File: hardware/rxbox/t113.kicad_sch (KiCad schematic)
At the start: 1 part, among them U1 T113-I

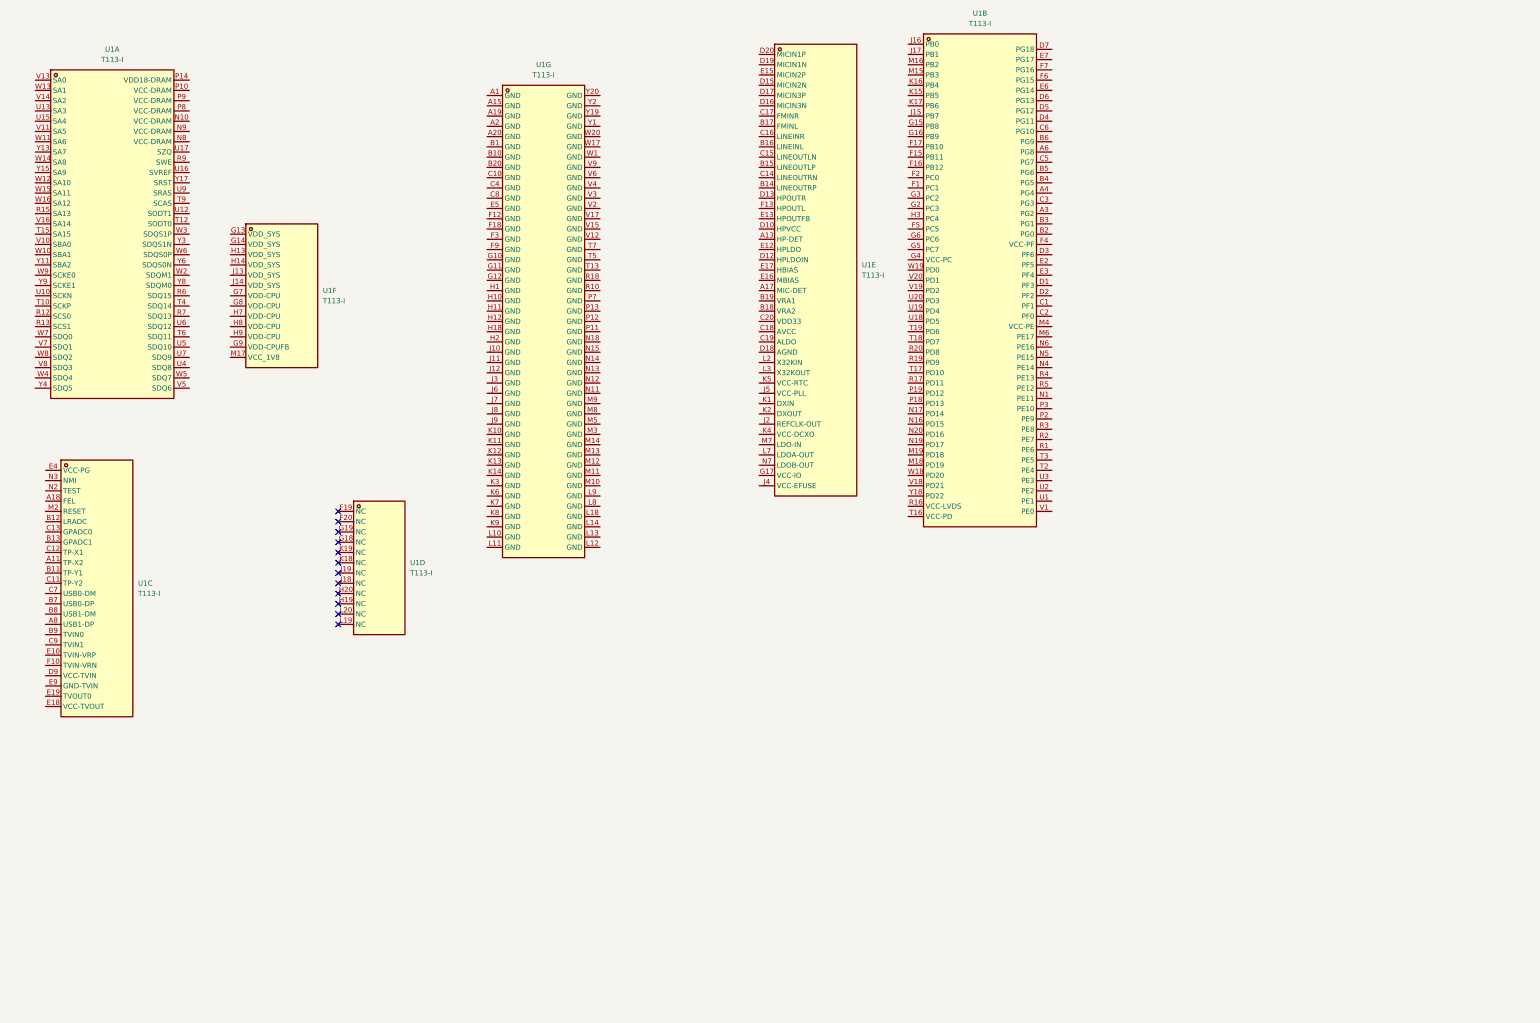
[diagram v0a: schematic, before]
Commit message: connect power + t113 sheets
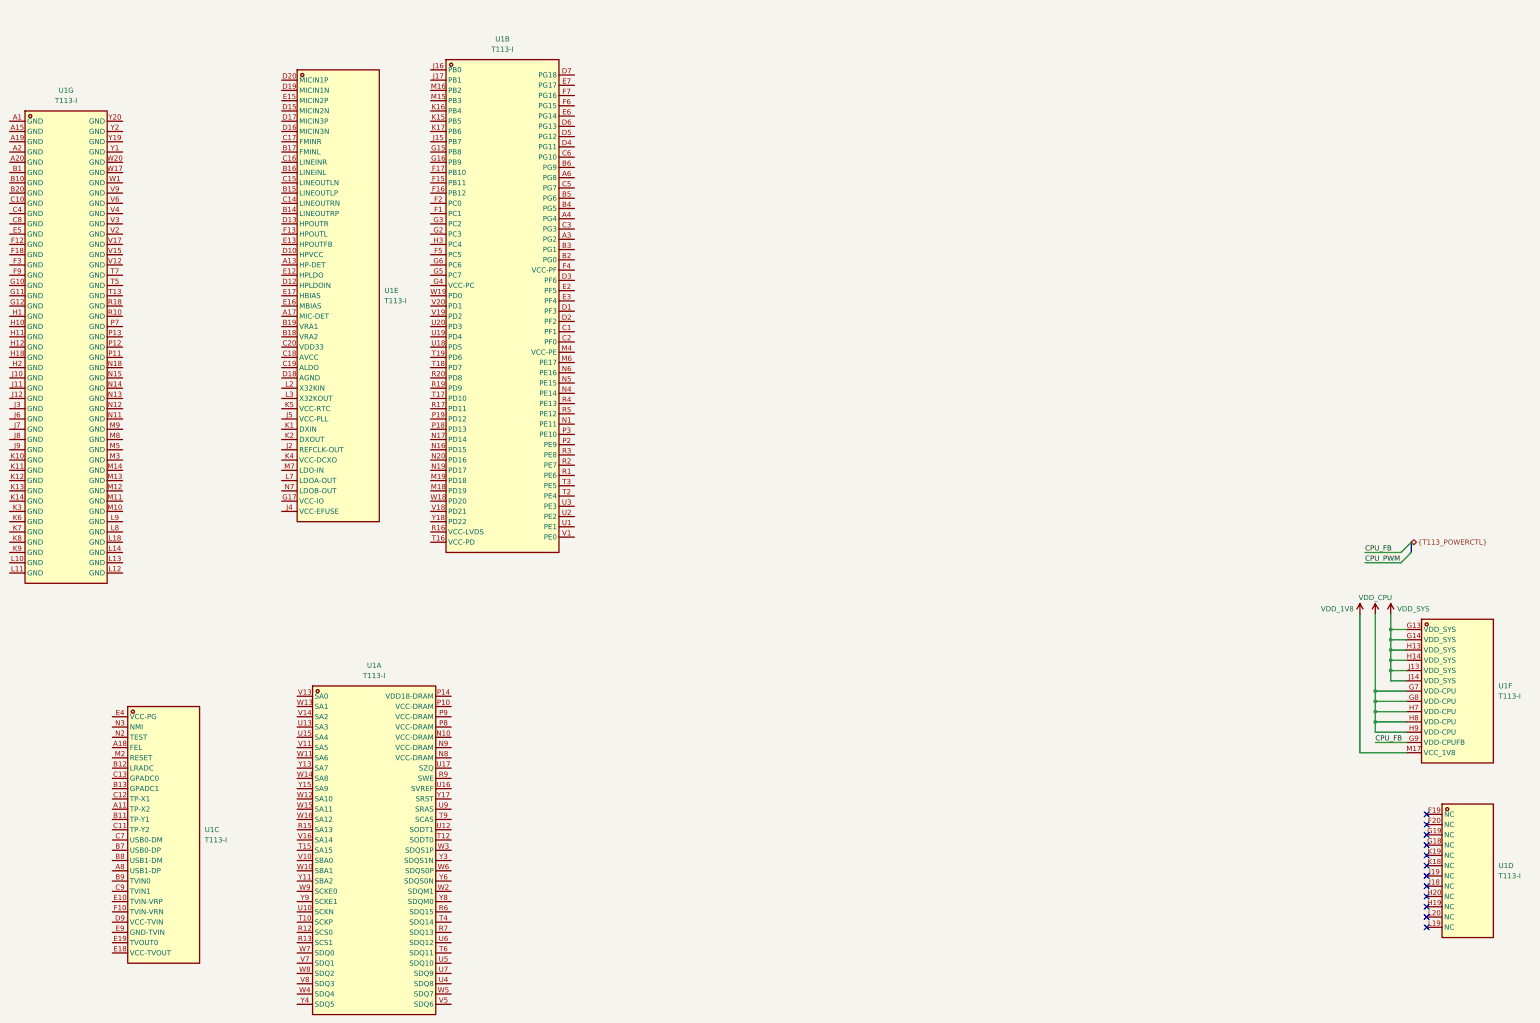
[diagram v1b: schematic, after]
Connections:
- net VDD_SYS: now reaches U1.G13 (VDD_SYS)
- net VDD_SYS: now also U1.G14 (VDD_SYS), U1.H13 (VDD_SYS), U1.H14 (VDD_SYS), U1.J13 (VDD_SYS), U1.J14 (VDD_SYS)
- net VDD_CPU: now reaches U1.G7 (VDD-CPU)
- net VDD_CPU: now also U1.G8 (VDD-CPU), U1.H7 (VDD-CPU), U1.H8 (VDD-CPU), U1.H9 (VDD-CPU)
- net CPU_FB: now reaches U1.G9 (VDD-CPUFB)
- net VDD_1V8: now reaches U1.M17 (VCC_1V8)
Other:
- moved on the sheet: U1A, U1B, U1C, U1D, U1E, U1F, U1G

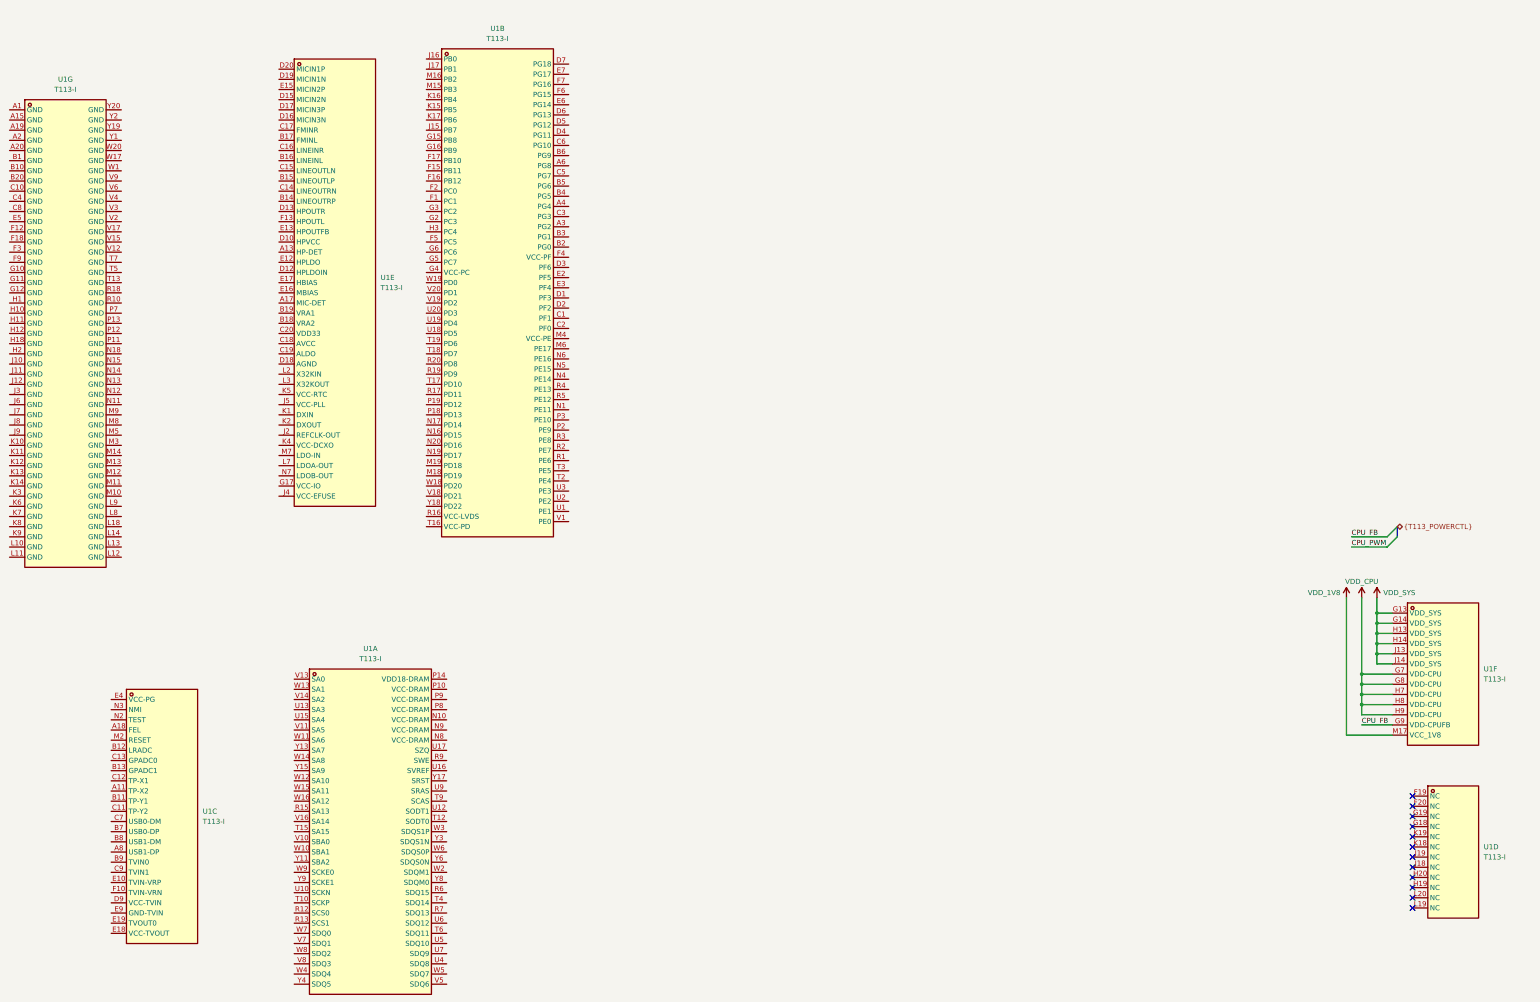
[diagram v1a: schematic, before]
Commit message: finish up power, start wifi
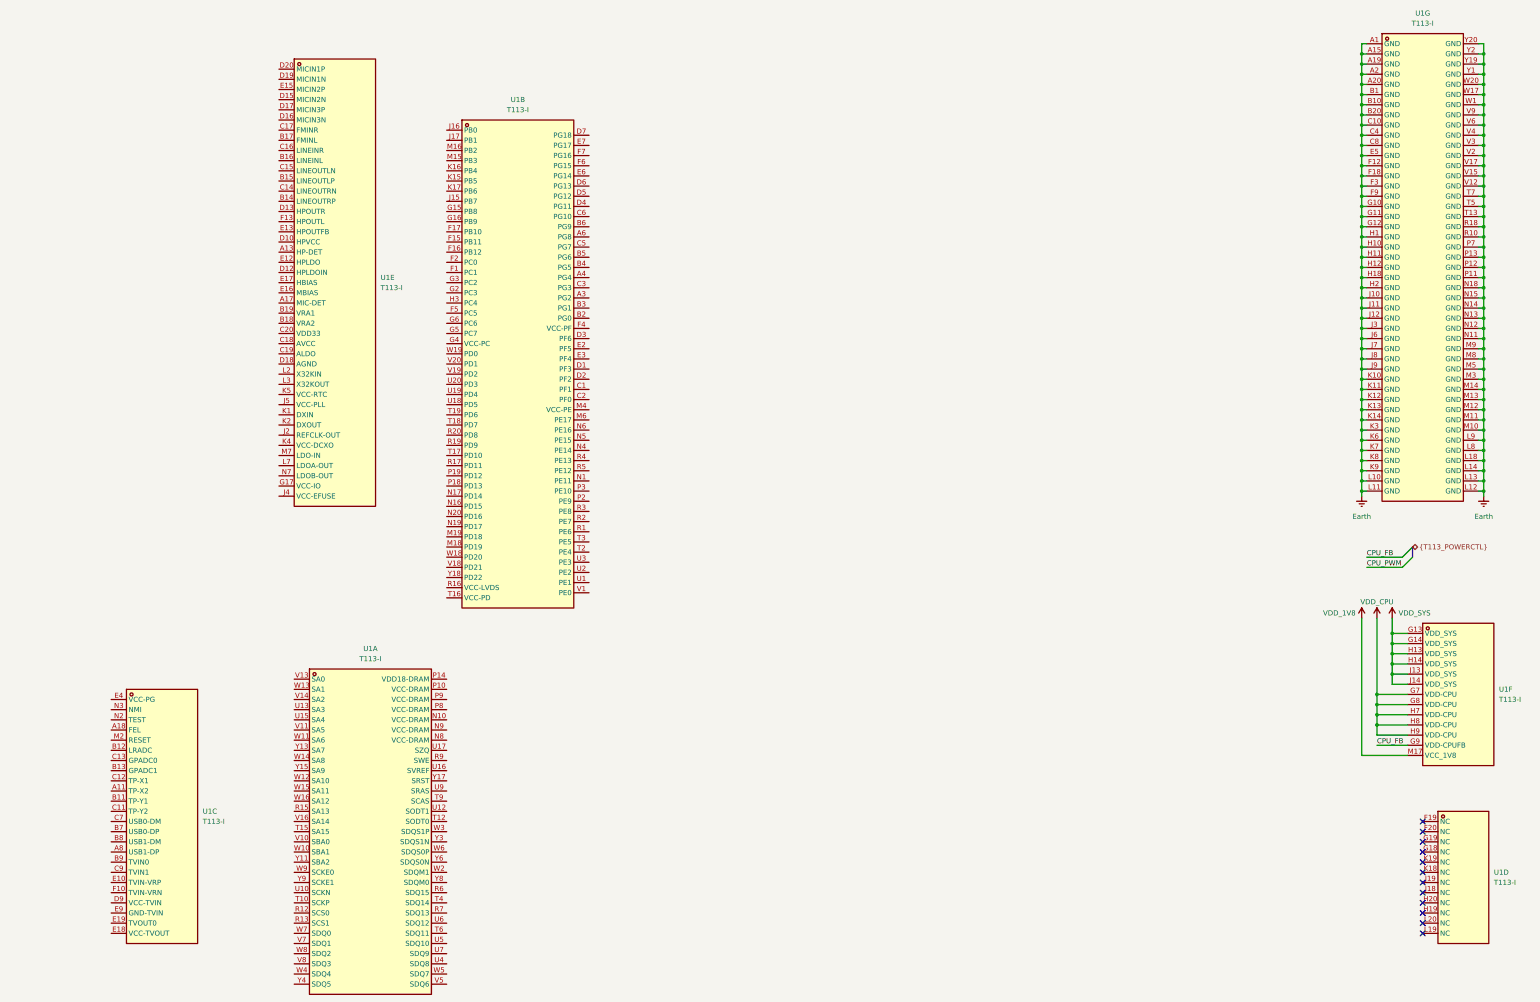
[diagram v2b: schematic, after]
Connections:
- net Earth: now reaches U1.A1 (GND)
- net Earth: now also U1.A15 (GND), U1.A19 (GND), U1.A2 (GND), U1.A20 (GND), U1.B1 (GND), U1.B10 (GND), U1.B20 (GND), U1.C10 (GND), U1.C4 (GND), U1.C8 (GND), U1.E5 (GND), U1.F12 (GND), U1.F18 (GND), U1.F3 (GND), U1.F9 (GND), U1.G10 (GND), U1.G11 (GND), U1.G12 (GND), U1.H1 (GND), U1.H10 (GND), U1.H11 (GND), U1.H12 (GND), U1.H18 (GND), U1.H2 (GND), U1.J10 (GND), U1.J11 (GND), U1.J12 (GND), U1.J3 (GND), U1.J6 (GND), U1.J7 (GND), U1.J8 (GND), U1.J9 (GND), U1.K10 (GND), U1.K11 (GND), U1.K12 (GND), U1.K13 (GND), U1.K14 (GND), U1.K3 (GND), U1.K6 (GND), U1.K7 (GND), U1.K8 (GND), U1.K9 (GND), U1.L10 (GND), U1.L11 (GND), U1.L12 (GND), U1.L13 (GND), U1.L14 (GND), U1.L18 (GND), U1.L8 (GND), U1.L9 (GND), U1.M10 (GND), U1.M11 (GND), U1.M12 (GND), U1.M13 (GND), U1.M14 (GND), U1.M3 (GND), U1.M5 (GND), U1.M8 (GND), U1.M9 (GND), U1.N11 (GND), U1.N12 (GND), U1.N13 (GND), U1.N14 (GND), U1.N15 (GND), U1.N18 (GND), U1.P11 (GND), U1.P12 (GND), U1.P13 (GND), U1.P7 (GND), U1.R10 (GND), U1.R18 (GND), U1.T13 (GND), U1.T5 (GND), U1.T7 (GND), U1.V12 (GND), U1.V15 (GND), U1.V17 (GND), U1.V2 (GND), U1.V3 (GND), U1.V4 (GND), U1.V6 (GND), U1.V9 (GND), U1.W1 (GND), U1.W17 (GND), U1.W20 (GND), U1.Y1 (GND), U1.Y19 (GND), U1.Y2 (GND), U1.Y20 (GND)
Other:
- moved on the sheet: U1B, U1D, U1F, U1G

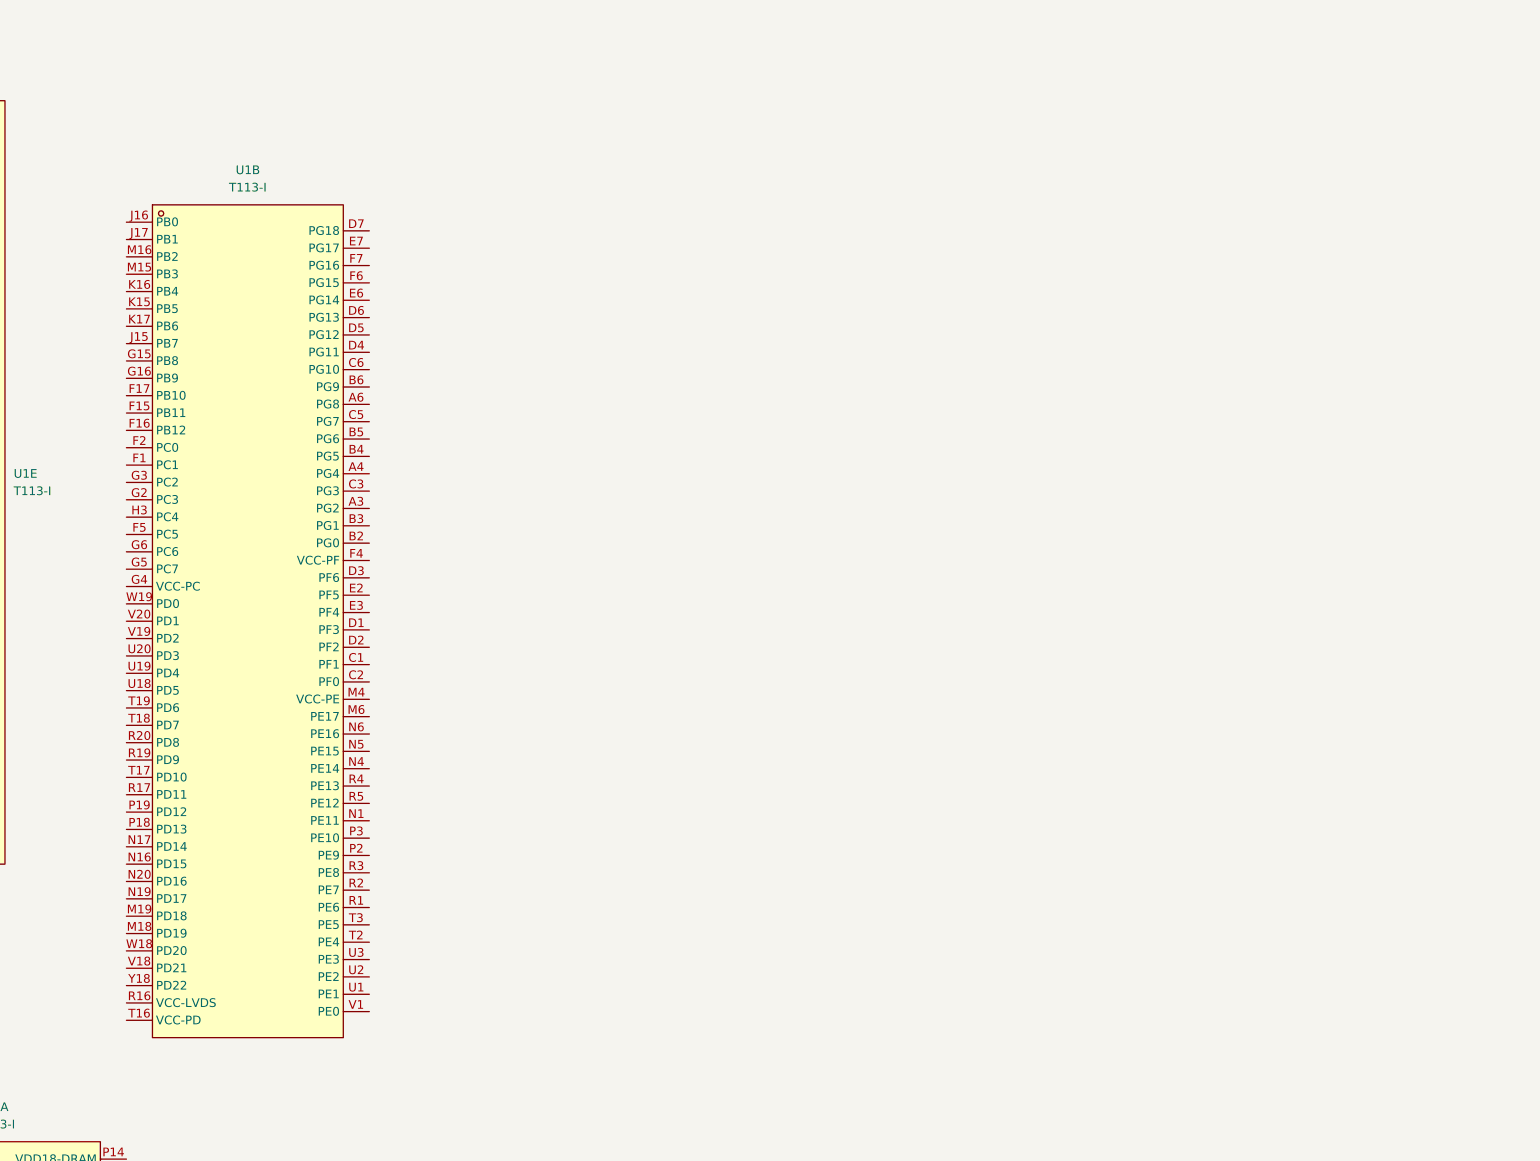
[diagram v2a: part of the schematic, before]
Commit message: wiring wifi + bt to t113
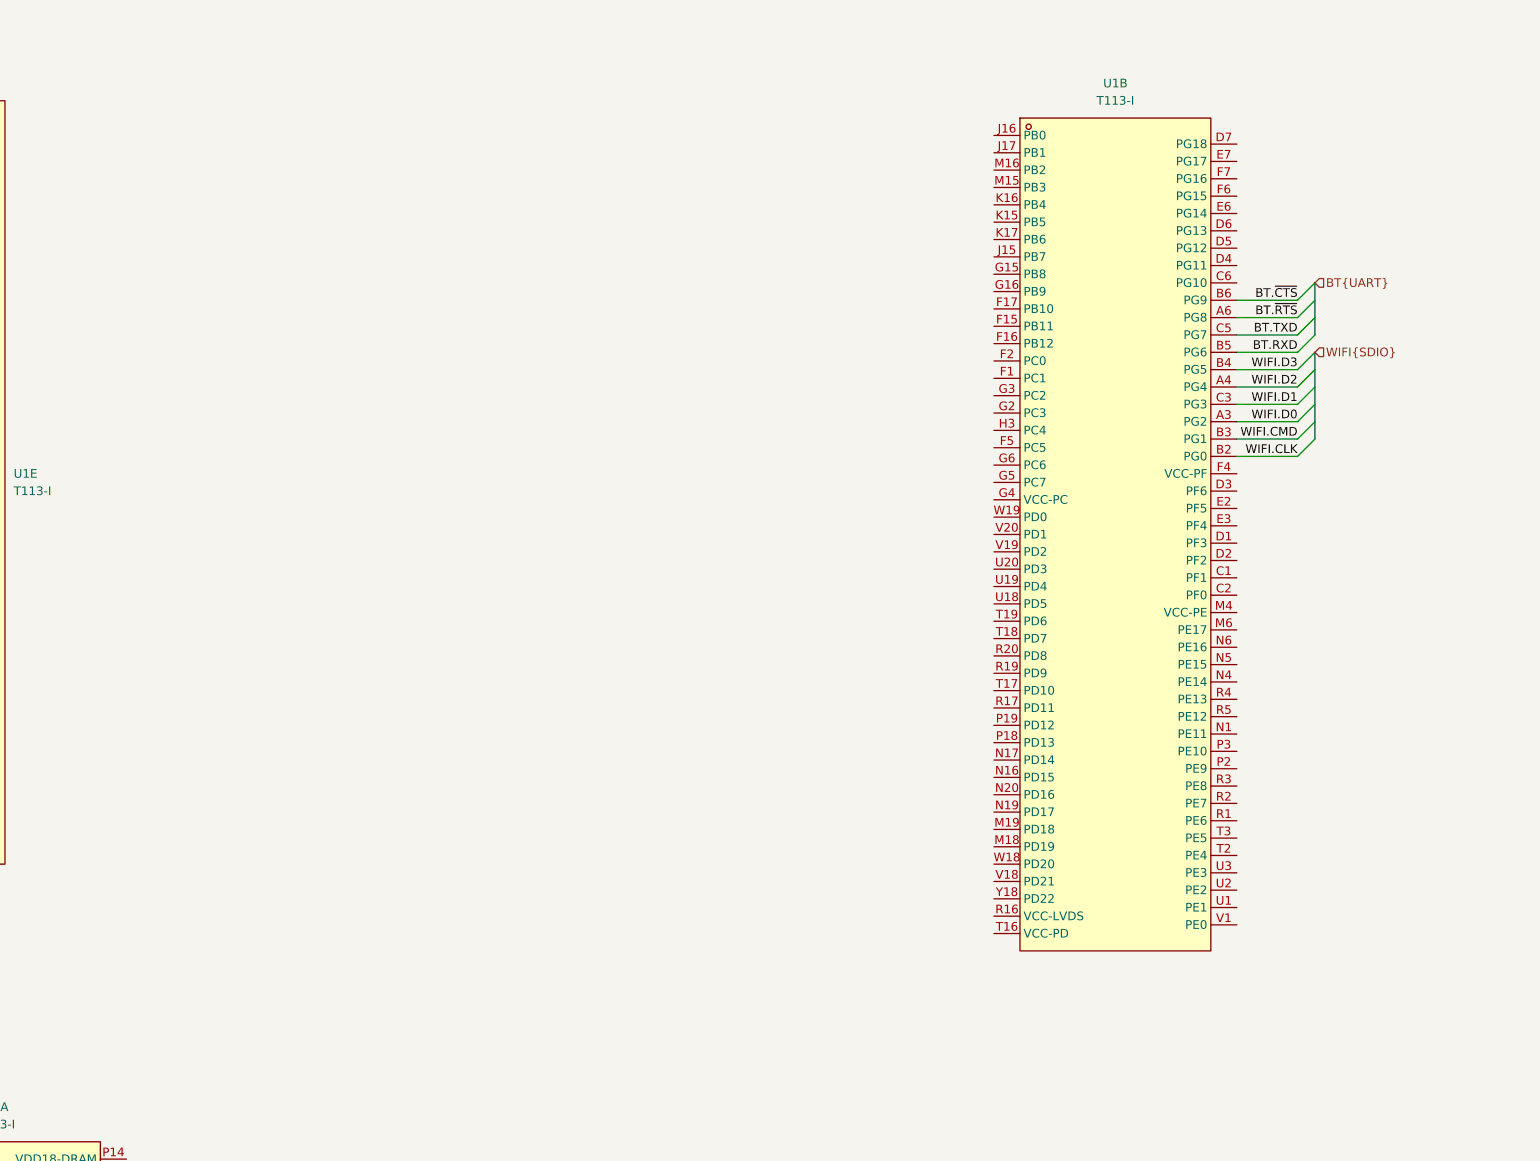
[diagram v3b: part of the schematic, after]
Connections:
- net WIFI.D0: now reaches U1.A3 (PG2)
- net WIFI.D2: now reaches U1.A4 (PG4)
- net BT.~{RTS}: now reaches U1.A6 (PG8)
- net WIFI.CLK: now reaches U1.B2 (PG0)
- net WIFI.CMD: now reaches U1.B3 (PG1)
- net WIFI.D3: now reaches U1.B4 (PG5)
- net BT.RXD: now reaches U1.B5 (PG6)
- net BT.~{CTS}: now reaches U1.B6 (PG9)
- net WIFI.D1: now reaches U1.C3 (PG3)
- net BT.TXD: now reaches U1.C5 (PG7)
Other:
- moved on the sheet: U1B
